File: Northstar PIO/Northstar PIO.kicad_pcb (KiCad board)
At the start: 2 copper layers, 76.3 x 139.9 mm, 43 parts, among them J1 Conn_01x02, J1A1 CONFIG.HDR., J2 Conn_01x02, J3 Conn_01x02, J4 Conn_01x02, J5 Conn_01x02, J6 Conn_01x02, J7 Conn_02x15_Odd_Even, P1 INPUT PORT, P2 OUTPUT PORT, U1B1 LS74, U1C1 LS74, U1D1 LS164, U2A1 LS32, U2B1 LS138, U2C1 LS175, U2D1 LS03, U2E1 LS367, U3A1 LS14, U3B1 7437, U3C1 LS373, U3D1 LS373

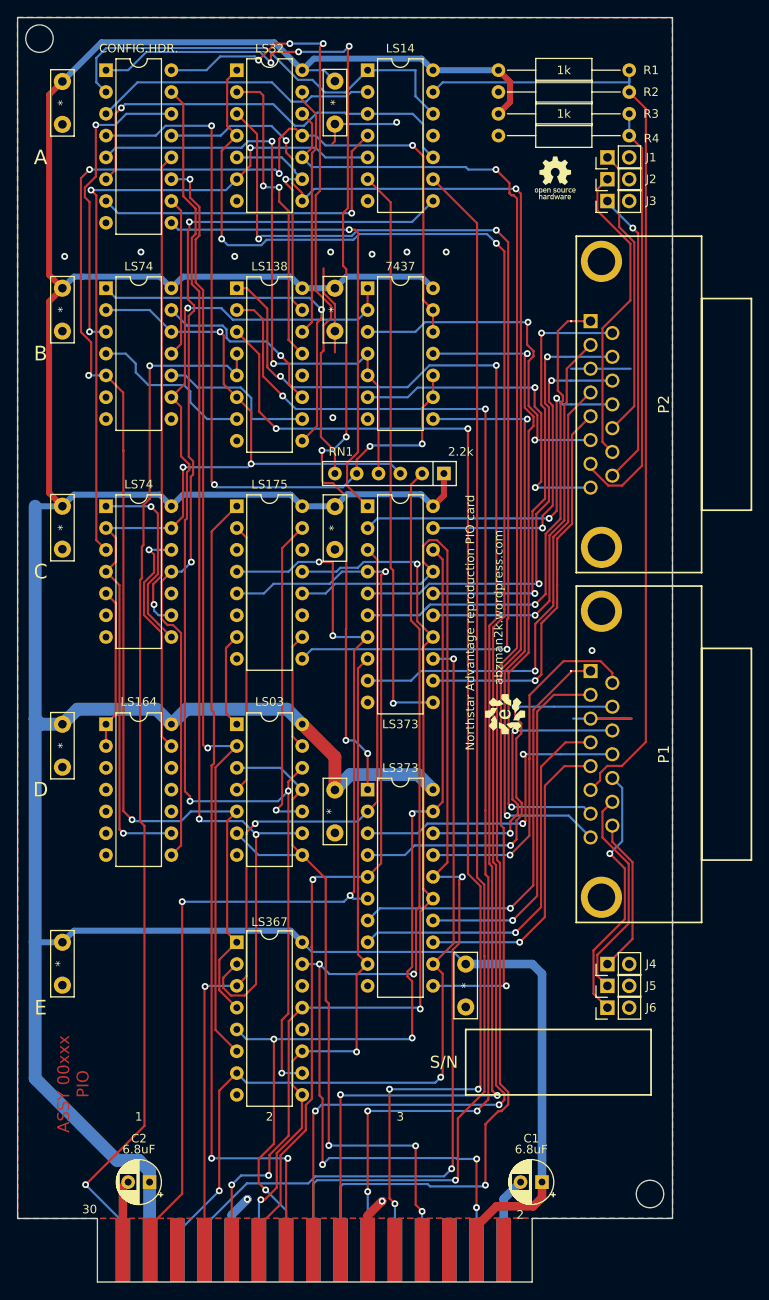
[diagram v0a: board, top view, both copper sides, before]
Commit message: fix pio problems discovered
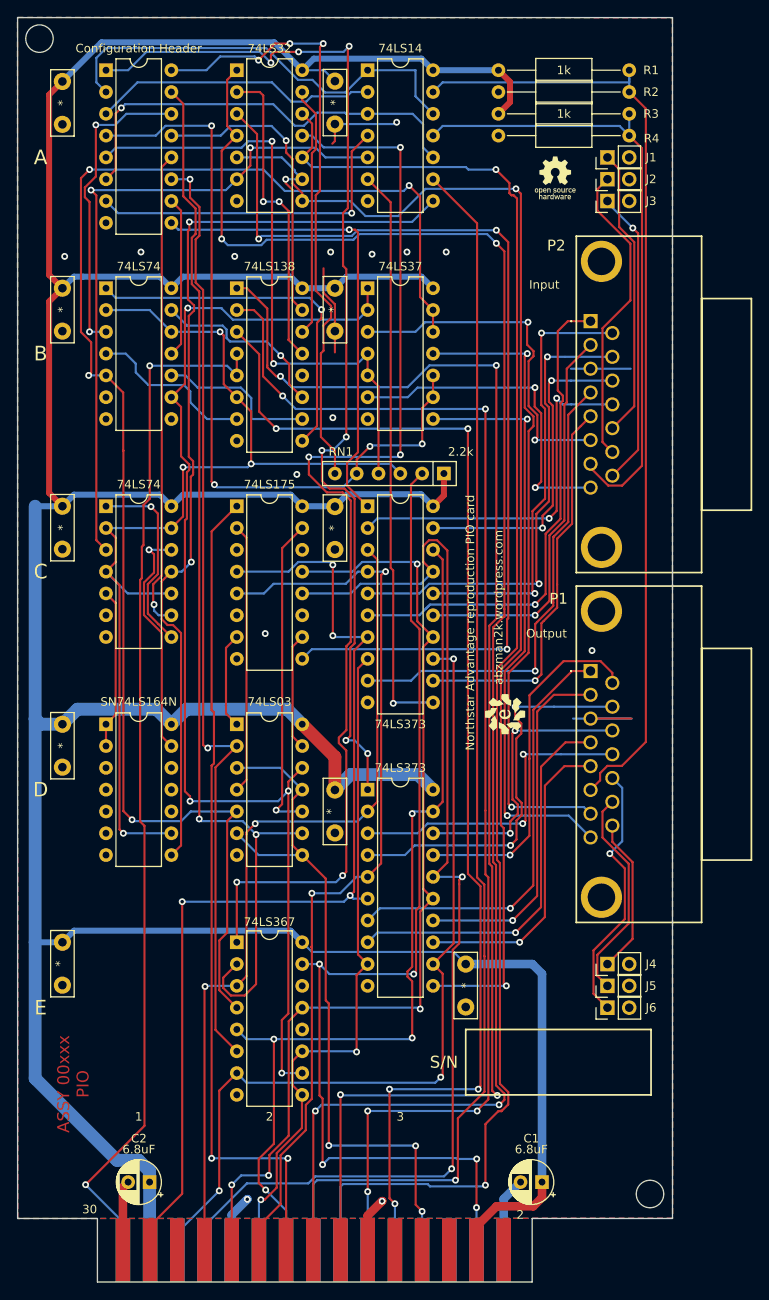
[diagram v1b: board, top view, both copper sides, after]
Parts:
- J1A1: value CONFIG.HDR. -> Configuration Header
- U1B1, U1C1: value LS74 -> 74LS74
- U1D1: value LS164 -> SN74LS164N
- U2A1: value LS32 -> 74LS32
- U2B1: value LS138 -> 74LS138
- U2C1: value LS175 -> 74LS175
- U2D1: value LS03 -> 74LS03
- U2E1: value LS367 -> 74LS367
- U3A1: value LS14 -> 74LS14
- U3B1: value 7437 -> 74LS37
- U3C1, U3D1: value LS373 -> 74LS373
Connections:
- net Net-(U1B1-Pad9) renamed /OUT FLAG
- P1 pad MH1: GND -> (no net)
- P1 pad MH2: GND -> (no net)
- P2 pad MH1: GND -> (no net)
- P2 pad MH2: GND -> (no net)
- U1C1 pad 10: unconnected-(U1C1-Pad10) -> /PUP
- U2A1 pad 11: /IN FLAG -> //READ STATUS
- U2E1 pad 1: /IN FLAG -> //READ STATUS
- U3A1 pad 11: unconnected-(U3A1-Pad11) -> //OUT ACK
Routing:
- net //READ STATUS: track 0.00 -> 131.0 mm, vias 0 -> 5
- net //OUT ACK: track 49.9 -> 73.7 mm
- net /IN FLAG: track 184.1 -> 174.1 mm, vias 5 -> 4
- net /PUP: track 115.4 -> 124.0 mm
- net //READ PI REGISTER: track 150.8 -> 152.2 mm
- net Net-(J1A1-Pad1): track 123.5 -> 124.7 mm
- net /IO4: track 107.0 -> 106.1 mm
- net GND: vias 12 -> 14
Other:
- board text added: "D0"
- board text added: "D1"
- board text added: "D2"
- board text added: "D3"
- board text added: "D4"
- board text added: "D5"
- board text added: "D6"
- board text added: "D7"
- board text added: "Gnd"
- board text added: "IN FLAG"
- board text added: "IN SPARE"
- board text added: "IN STROBE"
- board text added: "Input"
- board text added: "Input Port"
- board text added: "J1"
- board text added: "J2"
- board text added: "J3"
- board text added: "J4"
- board text added: "J5"
- board text added: "J6"
- board text added: "OUT ACK"
- board text added: "OUT FLAG"
- board text added: "OUT STROBE"
- board text added: "Output"
- board text added: "Output Port"

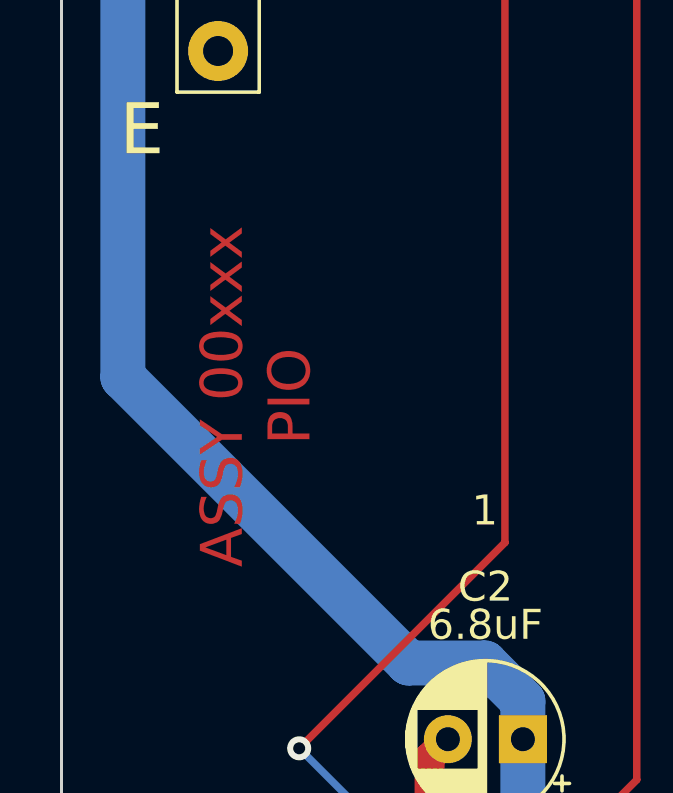
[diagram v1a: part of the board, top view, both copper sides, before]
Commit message: added some hard drive stuff and tweaked PIO silk
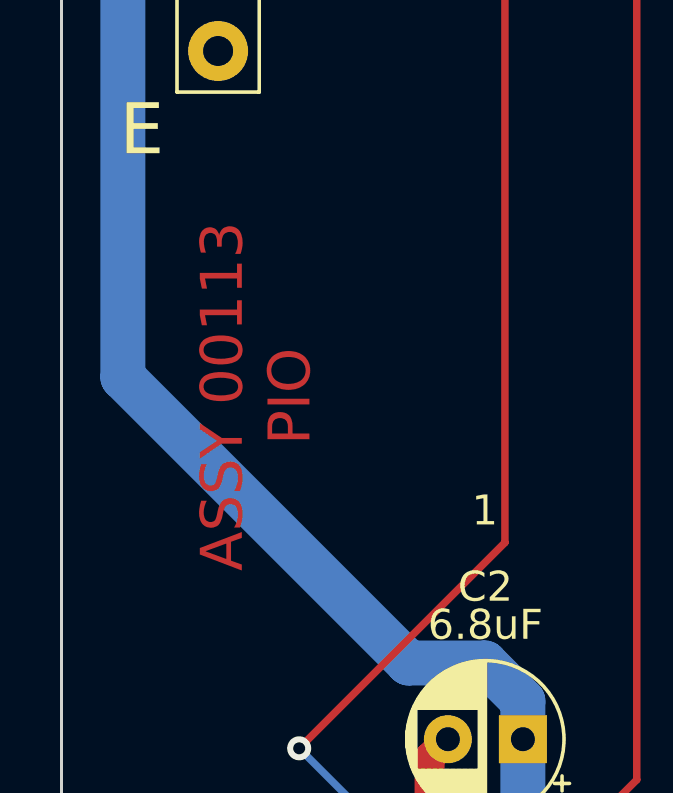
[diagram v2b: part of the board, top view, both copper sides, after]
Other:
- board text added: "ASSY 00113 PIO"
- board text removed: "ASSY 00xxx PIO"
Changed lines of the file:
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@@
   (gr_line (start 78.335373 27.805486) (end 154.635373 27.805486) (layer "Edge.Cuts") (width 0.1))
   (gr_line (start 87.635373 167.715486) (end 78.335373 167.715486) (layer "Edge.Cuts") (width 0.1))
-  (gr_text "ASSY 00xxx\nPIO" (at 84.825373 152.045486 90) (layer "F.Cu")
+  (gr_text "ASSY 00113\nPIO" (at 84.825373 152.045486 90) (layer "F.Cu")
     (effects (font (size 1.4 1.4) (thickness 0.2)))
   )
